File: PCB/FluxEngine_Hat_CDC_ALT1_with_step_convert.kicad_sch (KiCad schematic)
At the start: 8 parts, among them J1 CY8CKIT-059, J2 5V, J3 24V, P1 FDC_BUS_IBMPC, P2 FDC_BUS_CDC_alt1, U1 74HC00

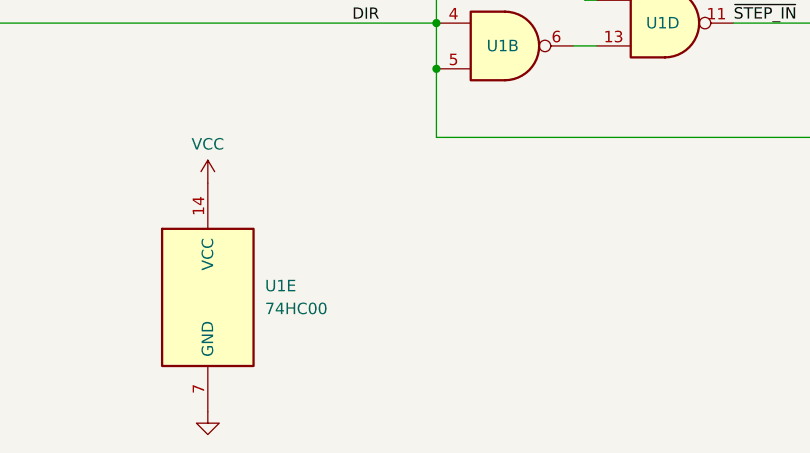
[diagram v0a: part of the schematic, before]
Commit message: WIP add step convert
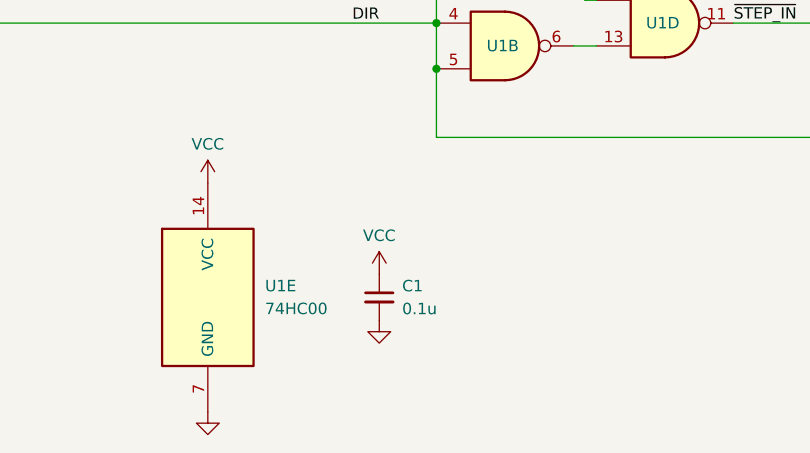
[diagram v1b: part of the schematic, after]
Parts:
- added C1: 0.1u, Capacitor_SMD:C_0805_2012Metric, symbol Device:C_Small
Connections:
- net GND: now also C1.2
- net VCC: now also C1.1
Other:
- title: FluxEngine_Hat for PC and CDC ALT1 -> FluxEngine_Hat for PC and CDC ALT1 with step convert
